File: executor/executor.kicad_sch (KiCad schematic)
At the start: 57 parts

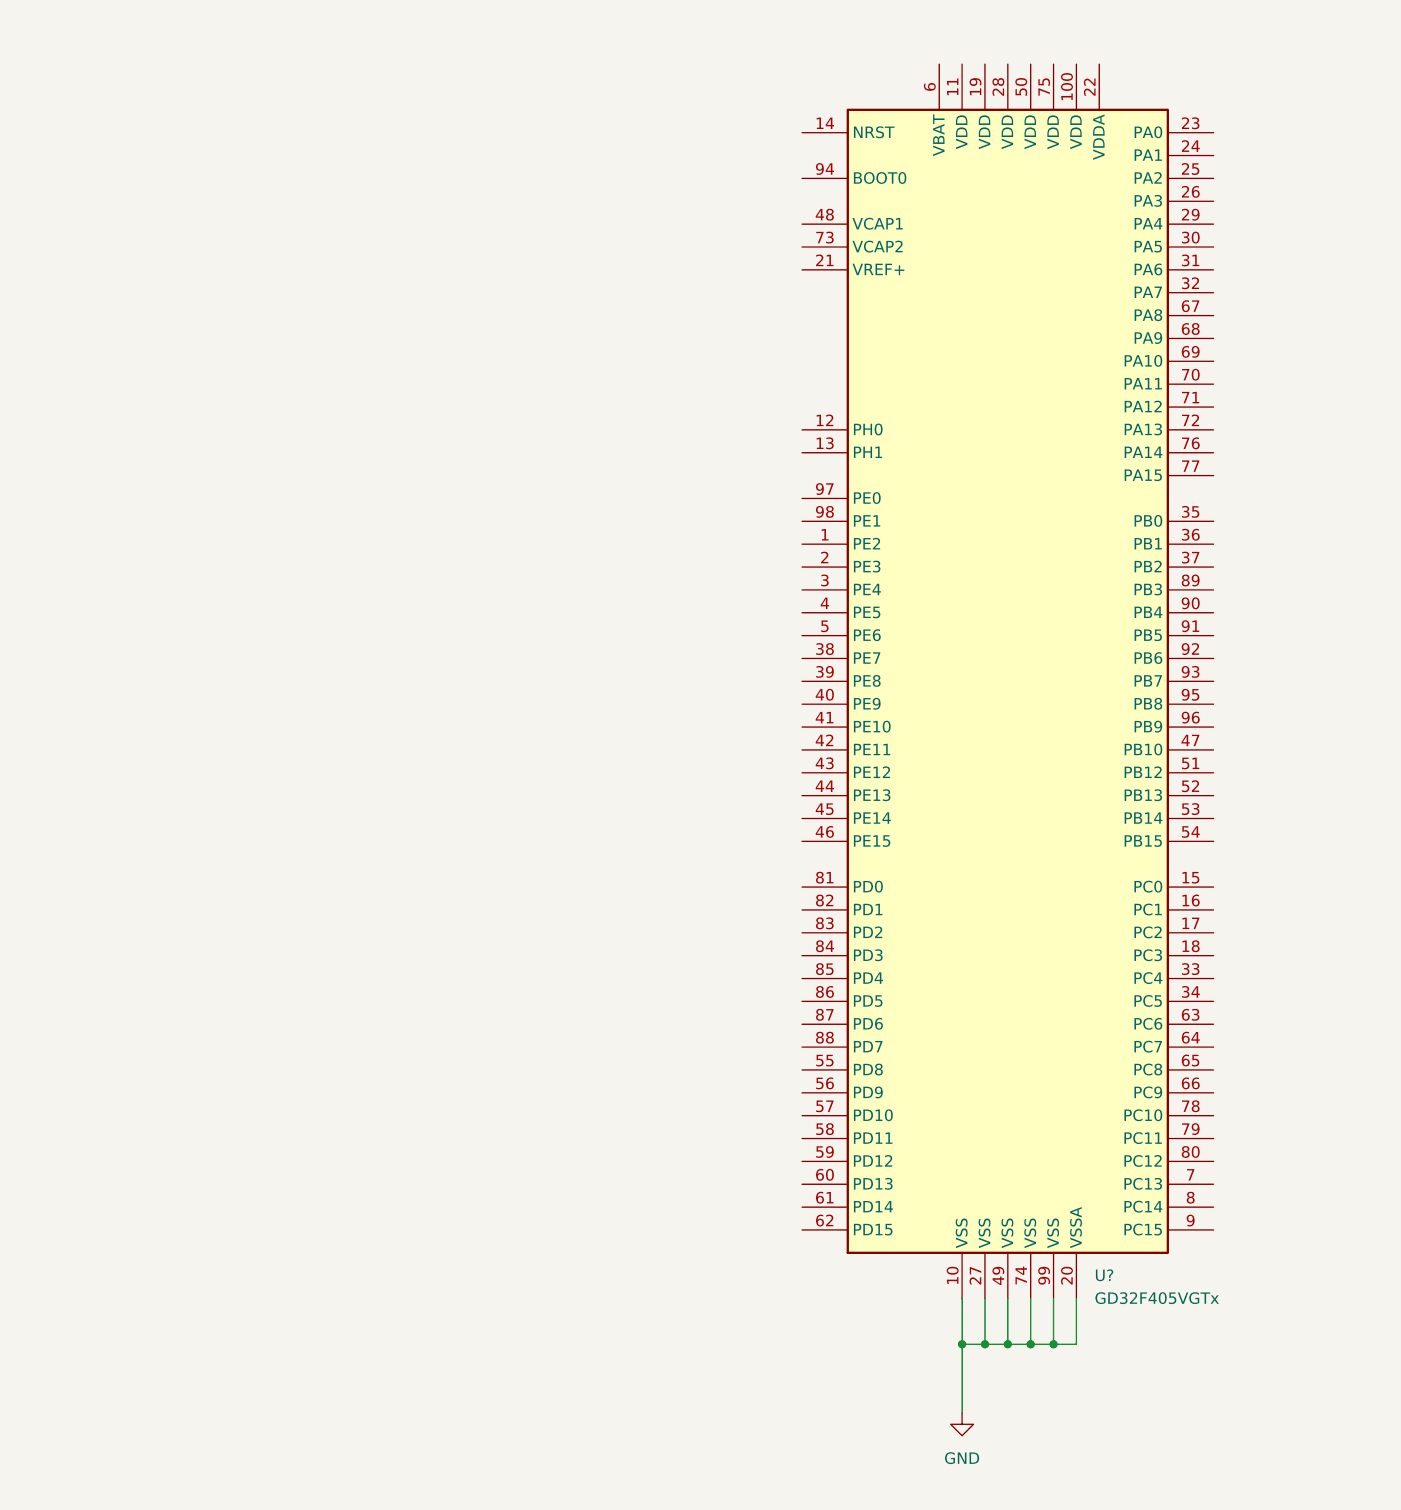
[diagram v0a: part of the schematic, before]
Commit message: [Fix] Fix library path
Signed-off-by: Homalozoa <nx.tardis@gmail.com>
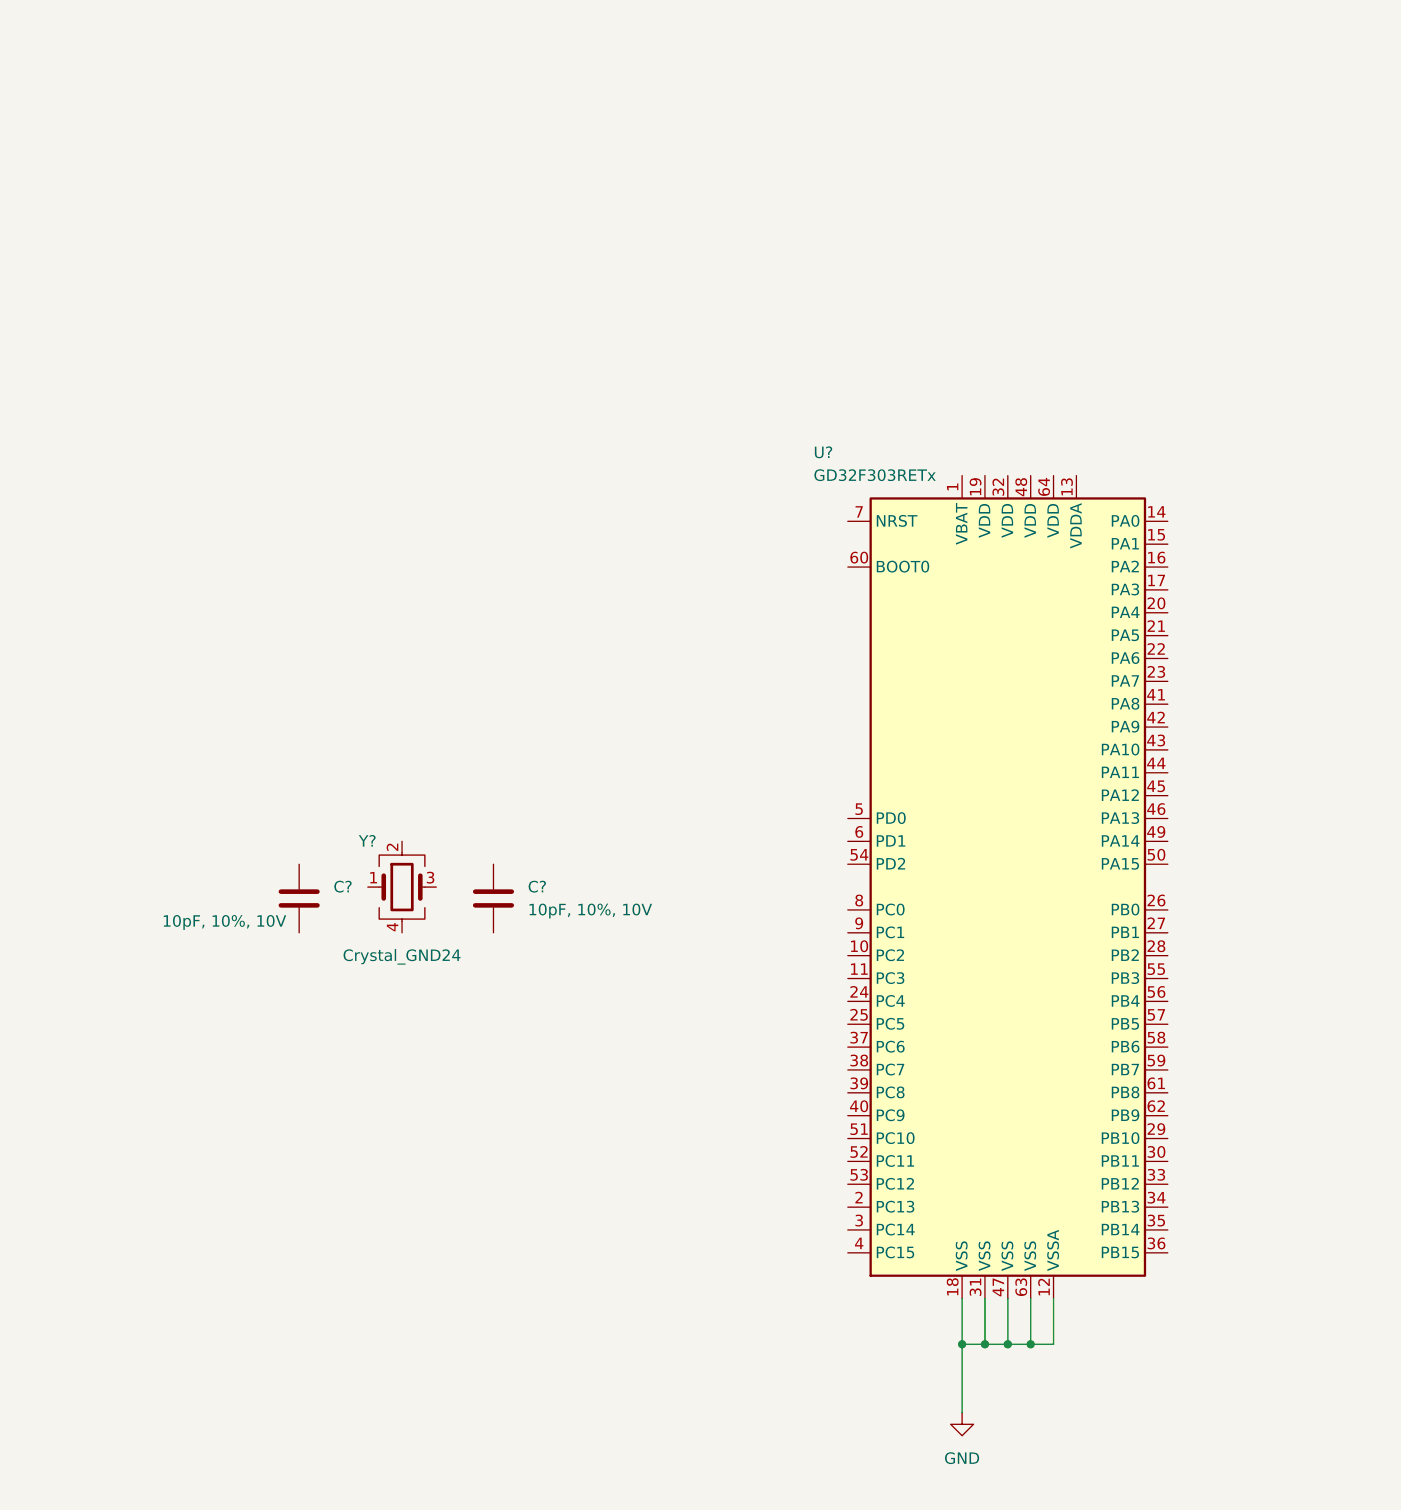
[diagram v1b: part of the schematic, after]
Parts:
- removed U?: GD32F405VGTx, Package_QFP:LQFP-100_14x14mm_P0.5mm, symbol Rolling_Custom:GD32F405VGTx
- added C? (x2): 10pF, 10%, 10V, Capacitor_SMD:C_0402_1005Metric, symbol Device:C
- added U?: GD32F303RETx, Package_QFP:LQFP-64_10x10mm_P0.5mm, symbol Rolling_Custom:GD32F303RETx
- added Y?: Crystal_GND24, symbol Device:Crystal_GND24
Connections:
- net GND: now also U?.12 (VSSA), U?.18 (VSS), U?.31 (VSS), U?.47 (VSS), U?.63 (VSS)

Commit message: [New] Update executor sch
Signed-off-by: Homalozoa <nx.tardis@gmail.com>
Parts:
- removed U?: BMI088, Rolling_Custom:PQFN50P450X300X100-16N, symbol Rolling_Custom:BMI088
- added C? (x16): 10uF, 20%, 50V, Capacitor_SMD:C_0805_2012Metric, symbol Device:C
- added C?: 10nF, 10%, 10V, Capacitor_SMD:C_0402_1005Metric, symbol Device:C
- added C? (x8): 100nF, 10%, 10V, Capacitor_SMD:C_0402_1005Metric, symbol Device:C
- added C? (x2): 10uF, 10%, 10V, Capacitor_SMD:C_0402_1005Metric, symbol Device:C
- added C? (x2): 10pF, 10%, 50V, Capacitor_SMD:C_0402_1005Metric, symbol Device:C
- added C? (x2): 10uF, 10%, 50V, Capacitor_SMD:C_0402_1005Metric, symbol Device:C
- added C?: 47uF, 10% 50V, symbol Device:C_Polarized_US
- added C?: 300nF, 10%, 50V, Capacitor_SMD:C_0402_1005Metric, symbol Device:C
- added C? (x2): 100pF, 10%, 10V, Capacitor_SMD:C_0402_1005Metric, symbol Device:C
- added C? (x2): 1uF, 10%, 10V, Capacitor_SMD:C_0402_1005Metric, symbol Device:C
- added C?: 100nF, 10%, 50V, Capacitor_SMD:C_0402_1005Metric, symbol Device:C
- added C?: 4.7uF, 10%, 10V, Capacitor_SMD:C_0402_1005Metric, symbol Device:C
- added C?: 10nF, 10%, 50V, Capacitor_SMD:C_0402_1005Metric, symbol Device:C
- added C?: 2.2uF, 10%, 10V, Capacitor_SMD:C_0402_1005Metric, symbol Device:C
- added C?: 100nnF, 10%, 10V, Capacitor_SMD:C_0402_1005Metric, symbol Device:C
- added D? (x2): 12V, symbol Device:D_TVS
- added D? (x2): BAV99, Package_TO_SOT_SMD:SOT-23, symbol Diode:BAV99
- added D?: Blue, LED_SMD:LED_0402_1005Metric, symbol Device:LED
- added L?: 20R, Inductor_SMD:L_0603_1608Metric, symbol Device:L
- added R? (x2): 2.2k, 5%, Resistor_SMD:R_0402_1005Metric, symbol Device:R_US
- added R? (x4): 100R, 5%, Resistor_SMD:R_0402_1005Metric, symbol Device:R_US
- added R? (x3): 0R, 5%, Resistor_SMD:R_0402_1005Metric, symbol Device:R_US
- added R? (x7): 10k, 5%, Resistor_SMD:R_0402_1005Metric, symbol Device:R_US
- added R?: 120R, Resistor_SMD:R_0402_1005Metric, symbol Device:R_US
- added R?: 33k, Resistor_SMD:R_0402_1005Metric, symbol Device:R_US
- added R?: 150k, 5%, Resistor_SMD:R_0402_1005Metric, symbol Device:R_US
- added R?: 3k, Resistor_SMD:R_0402_1005Metric, symbol Device:R_US
- added R?: 0, symbol Device:R_US
- added TP?: TEMP_BOARD, TestPoint:TestPoint_Pad_D2.0mm, symbol Connector:TestPoint
- added TP?: VSENSE, TestPoint:TestPoint_Pad_D2.0mm, symbol Connector:TestPoint
- added TP?: 3V3, TestPoint:TestPoint_Pad_D2.0mm, symbol Connector:TestPoint
- added TP?: UART_RX, TestPoint:TestPoint_Pad_D2.0mm, symbol Connector:TestPoint
- added TP?: SWDIO, TestPoint:TestPoint_Pad_D2.0mm, symbol Connector:TestPoint
- added TP?: 24V, TestPoint:TestPoint_Pad_D2.0mm, symbol Connector:TestPoint
- added TP?: UART_TX, TestPoint:TestPoint_Pad_D2.0mm, symbol Connector:TestPoint
- added TP?: SWCLK, TestPoint:TestPoint_Pad_D2.0mm, symbol Connector:TestPoint
- added U?: AS5047P-ATSM, Package_SO:TSSOP-14_4.4x5mm_P0.65mm, symbol Rolling_Custom:AS5047P-ATSM
- added U?: QMA7981, Package_LGA:LGA-12_2x2mm_P0.5mm, symbol Rolling_Custom:QMA7981
- added Y?: 40M, symbol Device:Crystal_GND24
- Y?: value Crystal_GND24 -> 8M
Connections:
- net DRV_SCLK is gone; now on net DRV_SCK: U?.28 (SCLK)
- net +24V: now also C?.1, C?.1, C?.1, C?.1, C?.1, C?.1, C?.1, C?.1, C?.1, C?.1, C?.1, C?.1, C?.1, C?.1, C?.1, C?.1, C?.1, C?.1, C?.1, R?.1, R?.1, TP?.1
- net +3V3: now also U?.1 (VBAT), U?.17 (VIO), U?.19 (VDD), U?.32 (VDD), U?.48 (VDD), U?.64 (VDD), C?.1, C?.1, C?.1, C?.1, C?.1, C?.1, C?.1, C?.1, C?.1, C?.1, C?.2, C?.2, D?.2 (A), D?.2 (A), D?.2 (A), L?.2, R?.1, R?.1, R?.1, R?.2, R?.2, TP?.1, U?.10 (SENB/SCS), U?.11 (VDD), U?.12 (VDD3V3), U?.3 (VDDIO), U?.7 (VDD)
- net CAN_H: now also C?.2, D?.1 (A1), R?.1
- net CAN_L: now also C?.2, D?.1 (A1), R?.2
- net DRV_SCS: now also U?.20 (PA4)
- net DRV_SDI: now also U?.23 (PA7)
- net DRV_SDO: now also U?.22 (PA6)
- net ENABLE: no longer U?.35 (INLA), U?.36 (INHB), U?.39 (INLC)
- net GND: now also C?.1, C?.1, Y?.2, Y?.4, C?.1, C?.1, C?.1, C?.1, C?.1, C?.1, C?.1, C?.1, C?.2, C?.2, C?.2, C?.2, C?.2, C?.2, C?.2, C?.2, C?.2, C?.2, C?.2, C?.2, C?.2, C?.2, C?.2, C?.2, C?.2, C?.2, C?.2, C?.2, C?.2, C?.2, C?.2, C?.2, C?.2, C?.2, C?.2, C?.2, C?.2, C?.2, C?.2, C?.2, D?.1 (K), D?.1 (K), D?.2 (A2), D?.2 (A2), R?.1, R?.2, R?.2, R?.2, R?.2, U?.13 (GND), U?.4 (RESV1), U?.5 (TEST), U?.8 (GNDIO), U?.9 (GND), Y?.2, Y?.4; no longer U?.12 (VSSA)
- net ISENSE_B: now also U?.9 (PC1)
- net ISENSE_C: now also U?.10 (PC2)
- net PWM_A: now also R?.2
- net PWM_B: now also U?.36 (INHB), R?.2; no longer U?.38 (INHC)
- net PWM_C: now also U?.38 (INHC), R?.2; no longer U?.37 (INLB)
- net MCU_OSC_IN: now reaches Y?.1
- net MCU_OSC_IN: now also C?.2, U?.5 (PD0)
- net MCU_OSC_OUT: now reaches Y?.3
- net MCU_OSC_OUT: now also C?.2, U?.6 (PD1)
- net at U?.23 (SOA): now also R?.2
- net TEMP_MOTOR: now reaches U?.11 (PC3)
- net VREF_D: now reaches U?.13 (VDDA)
- net VREF_D: now also C?.2, C?.2, L?.1
- net at U?.14 (PA0): now also R?.1
- net TEMP_BOARD: now reaches U?.15 (PA1)
- net TEMP_BOARD: now also C?.2, R?.1, R?.2, TP?.1
- net DRV_SCK: now reaches U?.21 (PA5)
- net ACC_INT1: now reaches U?.27 (PB1)
- net ACC_INT1: now also U?.5 (INT1)
- net ACC_INT2: now reaches U?.28 (PB2)
- net ACC_INT2: now also U?.6 (INT2)
- net ACC_SCL: now reaches U?.29 (PB10)
- net ACC_SCL: now also R?.1, U?.1 (SCL/AD0/SDO)
- net ACC_SDA: now reaches U?.30 (PB11)
- net ACC_SDA: now also R?.1, U?.2 (SDA/SDI/SDIO)
- net TCAN_SDI: now reaches U?.33 (PB12)
- net TCAN_SDI: now also U?.5 (SDI)
- net TCAN_SDO: now reaches U?.34 (PB13)
- net TCAN_SDO: now also U?.6 (SDO), R?.2
- net TCAN_SCK: now reaches U?.35 (PB14)
- net TCAN_SCK: now also U?.4 (SCLK)
- net TCAN_SCS: now reaches U?.36 (PB15)
- net TCAN_SCS: now also U?.7 (~{CS})
- net TCAN_RST: now reaches U?.37 (PC6)
- net TCAN_RST: now also U?.19 (RST)
- net TCAN_INT: now reaches U?.38 (PC7)
- net TCAN_INT: now also U?.8 (~{INT})
- net TCAN_WKRQ: now reaches U?.39 (PC8)
- net TCAN_WKRQ: now also U?.2 (~{WKRQ})
- net at U?.41 (PA8): now also R?.1
- net at U?.42 (PA9): now also R?.1
- net at U?.43 (PA10): now also R?.1
- net DRV_EN: now reaches U?.44 (PA11)
- net DRV_EN: now also U?.35 (INLA), U?.37 (INLB), U?.39 (INLC)
- net SWDIO: now reaches U?.46 (PA13)
- net SWDIO: now also TP?.1
- net SWCLK: now reaches U?.49 (PA14)
- net SWCLK: now also TP?.1
- net ECD_SCS: now reaches U?.50 (PA15)
- net ECD_SCS: now also U?.1 (CSN)
- net at U?.51 (PC10): now also R?.2
- net at U?.52 (PC11): now also R?.2
- net ECD_SCK: now reaches U?.55 (PB3)
- net ECD_SCK: now also U?.2 (CLK)
- net ECD_MISO: now reaches U?.56 (PB4)
- net ECD_MISO: now also U?.3 (MISO)
- net ECD_MOSI: now reaches U?.57 (PB5)
- net ECD_MOSI: now also U?.4 (MOSI)
- net at U?.60 (BOOT0): now also R?.1
- net NRST: now reaches U?.7 (NRST)
- net NRST: now also C?.1, R?.2
- net ISENSE_A: now reaches U?.8 (PC0)
- net ISENSE_A: now also D?.3 (K), R?.1
- net TCAN_OSC_IN: now reaches U?.1 (OSC1)
- net TCAN_OSC_IN: now also C?.2, Y?.1
- net TCAN_WAKE: now reaches U?.12 (WAKE)
- net TCAN_WAKE: now also R?.1
- net VCCOUT: now reaches U?.16 (VCCOUT)
- net VCCOUT: now also C?.1
- net at U?.18 (FLTR): now also C?.1
- net TCAN_OSC_OUT: now reaches U?.20 (OSC2)
- net TCAN_OSC_OUT: now also C?.2, Y?.3
- new net: D?.1 (K), R?.1
- new net: C?.2, R?.2, R?.2
- new net UART_RX: R?.1, TP?.1
- new net UART_TX: R?.1, TP?.1
- new net VREF_S: C?.1, C?.1, R?.2, U?.12 (VSSA)
- new net VSEN_BUS: D?.3 (K), R?.1, R?.2, R?.2, TP?.1
- no-connect marks 2 -> 11
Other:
- moved on the sheet: C?, D?, L?, R?, U?, Y?

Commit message: [New] Complete executor sch
Signed-off-by: Homalozoa <nx.tardis@gmail.com>
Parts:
- removed L?: 20R, Inductor_SMD:L_0603_1608Metric, symbol Device:L
- added D3: ESD56161D30, Rolling_Custom:DFN2x2-3L, symbol Rolling_Custom:ESD56161D30
- added J1: XT30PW(2+2), Rolling_Custom:XT30PW(2+2), symbol Rolling_Custom:XT30PW(2+2)
- added R18: 0, symbol Device:R_US
- D8, D9: renamed from D?; footprint (none) -> Package_DFN_QFN:Diodes_DFN1006-3
- gave numbers to parts that had none: 136
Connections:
- net +24V: now also D3.1 (K), D3.2 (K), J1.1 (VBUS)
- net +3V3: now also R18.1
- net CAN_H: now also J1.3 (CAN_H)
- net CAN_L: now also J1.4 (CAN_L)
- net GND: now also D3.3 (A), J1.2 (GND)
- net VREF_D: now also R18.2
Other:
- moved on the sheet: C1, C11, C13, C14, C15, C18, C19, C2, C20, C21, C22, C3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

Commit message: [New] complete executor PCB layout
Signed-off-by: Homalozoa <nx.tardis@gmail.com>
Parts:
- removed NT2, NT3, NT4, NT5: NetTie, symbol Device:NetTie_2
- removed R18: 0, symbol Device:R_US
- removed R20, R21: 100R, 5%, Resistor_SMD:R_0402_1005Metric, symbol Device:R_US
- removed R27, R37: 10k, 5%, Resistor_SMD:R_0402_1005Metric, symbol Device:R_US
- removed TP2: UART_TX, TestPoint:TestPoint_Pad_D2.0mm, symbol Connector:TestPoint
- removed TP3: UART_RX, TestPoint:TestPoint_Pad_D2.0mm, symbol Connector:TestPoint
- removed TP6: 24V, TestPoint:TestPoint_Pad_D2.0mm, symbol Connector:TestPoint
- added C33: 100nF, 10%, 10V, Capacitor_SMD:C_0402_1005Metric, symbol Device:C
- added L2: 20R, Resistor_SMD:R_0402_1005Metric, symbol Device:L_Ferrite
- added R17: 10k, 5%, Resistor_SMD:R_0402_1005Metric, symbol Device:R_US
- added TP10: C, TestPoint:TestPoint_Plated_Hole_D2.0mm, symbol Connector:TestPoint
- added TP13: NTC+, TestPoint:TestPoint_Loop_D1.80mm_Drill1.0mm_Beaded, symbol Connector:TestPoint
- added TP14: NTC-, TestPoint:TestPoint_Loop_D1.80mm_Drill1.0mm_Beaded, symbol Connector:TestPoint
- C22: footprint (none) -> Capacitor_SMD:CP_Elec_8x6.2
- D1: footprint Rolling_Custom:DIODFN62X32X33-2N -> Diode_SMD:D_SOD-923
- D8, D9: footprint Package_DFN_QFN:Diodes_DFN1006-3 -> Diode_SMD:D_SOD-323
- NT1: footprint (none) -> NetTie:NetTie-2_SMD_Pad0.5mm
- R1, R12, R13, R19, R2, R7, R8: footprint (none) -> Resistor_SMD:R_0402_1005Metric
- TP4, TP5: footprint TestPoint:TestPoint_Pad_D2.0mm -> TestPoint:TestPoint_Pad_D1.5mm
- TP7: value VSENSE -> A; footprint TestPoint:TestPoint_Pad_D2.0mm -> TestPoint:TestPoint_Plated_Hole_D2.0mm
- TP8: value TEMP_BOARD -> B; footprint TestPoint:TestPoint_Pad_D2.0mm -> TestPoint:TestPoint_Plated_Hole_D2.0mm
- Y1, Y2: footprint (none) -> Oscillator:Oscillator_SMD_EuroQuartz_XO32-4Pin_3.2x2.5mm
- renumbered C33 to C34, C34 to C35, C39 to C37, C35 to C38, C37 to C39, C38 to C40, C40 to C41, C41 to C42, C42 to C43, C43 to C44, C44 to C45, C45 to C46, C46 to C47, C49 to C48, C50 to C49, C47 to C50, C48 to C51, C51 to C52, C54 to C53, C56 to C54, C57 to C55, C52 to C56, C53 to C57, C55 to C58, C58 to C59, C61 to C60, C59 to C61, C60 to C63, C63 to C64, C64 to C65, C65 to C66, R17 to R18, R23 to R20, R24 to R21, R25 to R22, R26 to R23, R22 to R27, R33 to R32, R32 to R33, R35 to R36, R36 to R37, U6 to U4, U4 to U5, U5 to U6
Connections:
- net ENABLE is gone; now on net DRV_EN: U2.30 (ENABLE)
- net IBN is gone; now on net GNDA: C32.2, U2.11 (SNB)
- net ICN is gone; now on net GNDA: C35.2, U2.20 (SNC)
- net +3V3: now also L2.1, R17.1
- net A: now also Q1.2, Q1.3, TP7.1
- net ACC_INT1: now also U3.28 (PB2); no longer U3.27 (PB1)
- net ACC_INT2: now also U3.27 (PB1); no longer U3.28 (PB2)
- net ACC_SCL: now also U6.12 (SCL); no longer U6.1 (SCL/AD0/SDO)
- net B: now also Q3.2, Q3.3, TP8.1
- net C: now also Q5.2, Q5.3, TP10.1
- net GND: now also NT1.1, U4.21 (BTM), U4.22 (HOLE_22), U4.23 (HOLE_23), U4.24 (HOLE_24), U4.25 (HOLE_25), C33.1, TP14.1; no longer C1.2, C11.2, C13.2, C14.2, C15.2, C17.1, C18.2, C19.2, C2.2, C20.2, C21.2, C22.2, C24.2, C26.2, C28.2, C3.2, C30.2, C31.2, C34.2, C36.2, C4.2, C5.2, C7.2, C8.2, C9.2, D3.3 (A), J1.2 (GND), NT1.2, Q2.1, R11.1, R16.2, R4.2, R9.2, U1.2 (GND), U2.32 (AGND)
- net IBP: now also C25.1, Q4.1, Q4.2, Q4.3, R9.1
- net ICP: now also C29.1, Q6.1, Q6.2, Q6.3, R16.1
- net ISENSE_A: now also U3.10 (PC2); no longer U3.8 (PC0)
- net ISENSE_C: now also U3.8 (PC0); no longer U3.10 (PC2)
- net PWM_B: now also R30.2; no longer R29.2
- net PWM_C: now also R29.2; no longer R30.2
- net TEMP_BOARD: no longer TP8.1
- net TEMP_MOTOR: now also C33.2, R17.2, TP13.1
- net VREF_D: now also L2.2
- net VSEN_BUS: no longer TP7.1
- net GNDA: now reaches Q2.2
- net GNDA: now also C1.2, C11.2, C13.2, C14.2, C15.2, C17.1, C18.2, C19.2, C2.2, C20.2, C21.2, C22.2, C24.2, C26.2, C28.2, C3.2, C30.2, C31.2, C34.2, C36.2, C4.2, C5.2, C7.2, C8.2, C9.2, D3.3 (A), J1.2 (GND), NT1.2, Q2.1, Q2.3, R11.1, R16.2, R4.2, R9.2, U1.2 (GND), U2.10 (SNA), U2.32 (AGND), U2.9 (SPA)
- removed net IAN: NT1.1, U2.10 (SNA), U2.9 (SPA)
- no-connect marks 11 -> 30
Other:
- moved on the sheet: C38, C39, C40, C41, C42, C43, C44, C45, C46, C47, C50, C51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

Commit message: [New] Complete executor ver 0.1
Signed-off-by: Homalozoa <nx.tardis@gmail.com>
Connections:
- net PWM_B: now also R29.2; no longer R30.2
- net PWM_C: now also R30.2; no longer R29.2

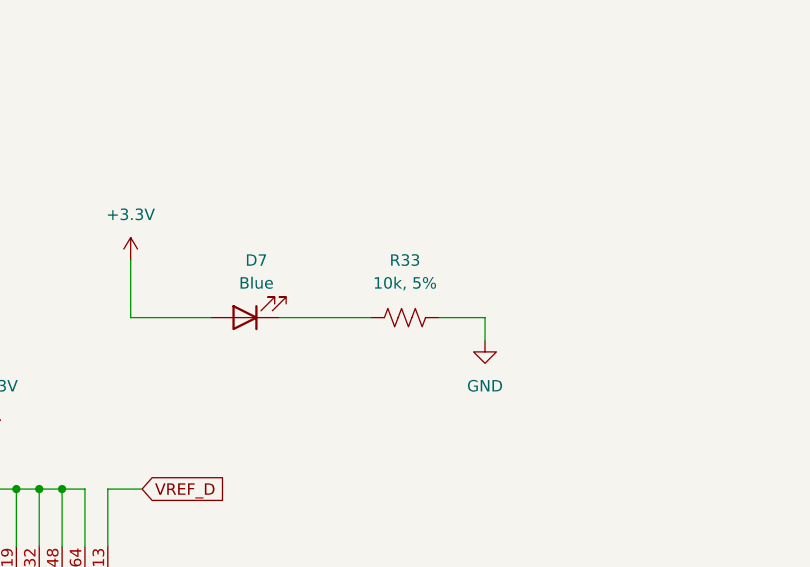
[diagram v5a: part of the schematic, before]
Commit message: [New] Add rpi_cm4 to lib
Signed-off-by: Homalozoa <nx.tardis@gmail.com>
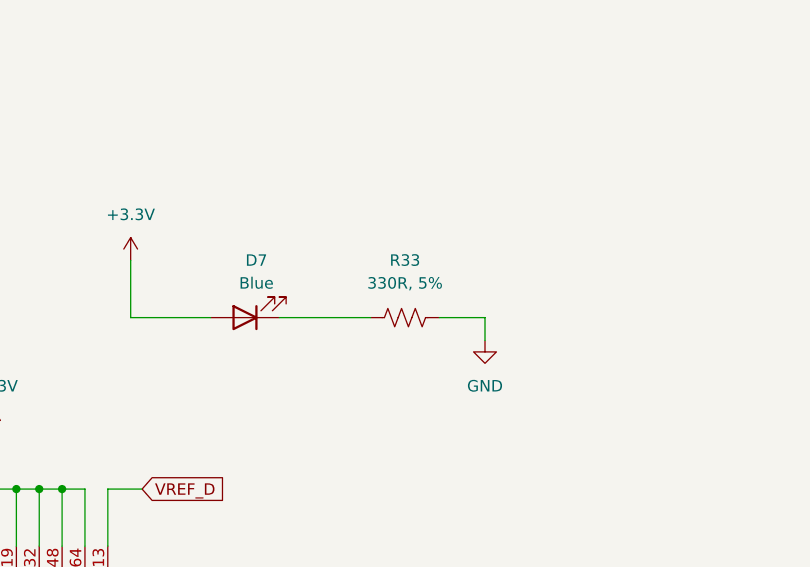
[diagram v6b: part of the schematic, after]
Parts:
- R33: value 10k, 5% -> 330R, 5%
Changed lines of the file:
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@@
     (in_bom yes) (on_board yes) (fields_autoplaced)
     (property "Reference" "R33" (id 0) (at 427.99 104.14 90))
-    (property "Value" "10k, 5%" (id 1) (at 427.99 106.68 90))
+    (property "Value" "330R, 5%" (id 1) (at 427.99 106.68 90))
     (property "Footprint" "Resistor_SMD:R_0402_1005Metric" (id 2) (at 428.244 109.474 90)
       (effects (font (size 1.27 1.27)) hide)
@@
     )
     (path "/71864906-2d8f-4141-b0ba-1609faa900a9"
-      (reference "R33") (unit 1) (value "10k, 5%") (footprint "Resistor_SMD:R_0402_1005Metric")
+      (reference "R33") (unit 1) (value "330R, 5%") (footprint "Resistor_SMD:R_0402_1005Metric")
     )
     (path "/a5779508-5cae-439a-b00e-8694b614cba2"
